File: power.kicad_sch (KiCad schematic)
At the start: 38 parts, among them IC3 LP5912-3.3DRVR, U12 BQ24075RGT, U2 LP5907SNX-1.8/NOPB, U3 LP5907SNX-3.3/NOPB, U4 LP5907SNX-1.8/NOPB, U6 LP5907SNX-3.3/NOPB, U7 LP5907SNX-3.3/NOPB

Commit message: segmented schematci
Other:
- note added: "BATTERY"
- note added: "BMS"
- note added: "REGULATORS"
- moved on the sheet: BT1, IC3

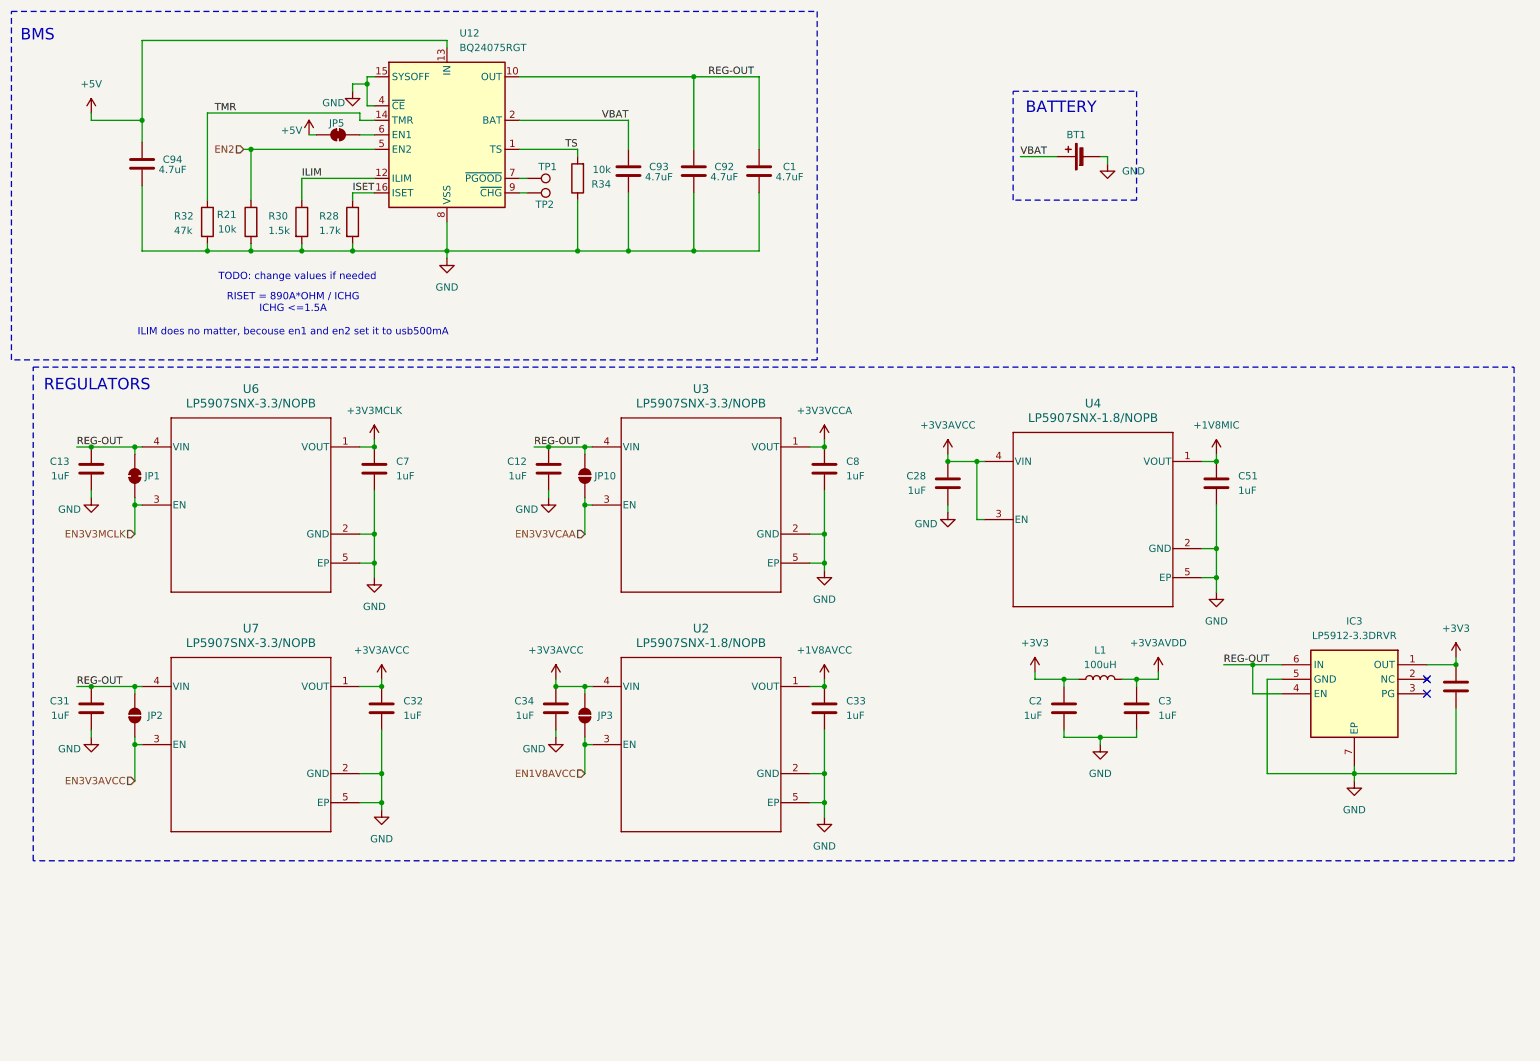
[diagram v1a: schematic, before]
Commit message: reannotated schematic
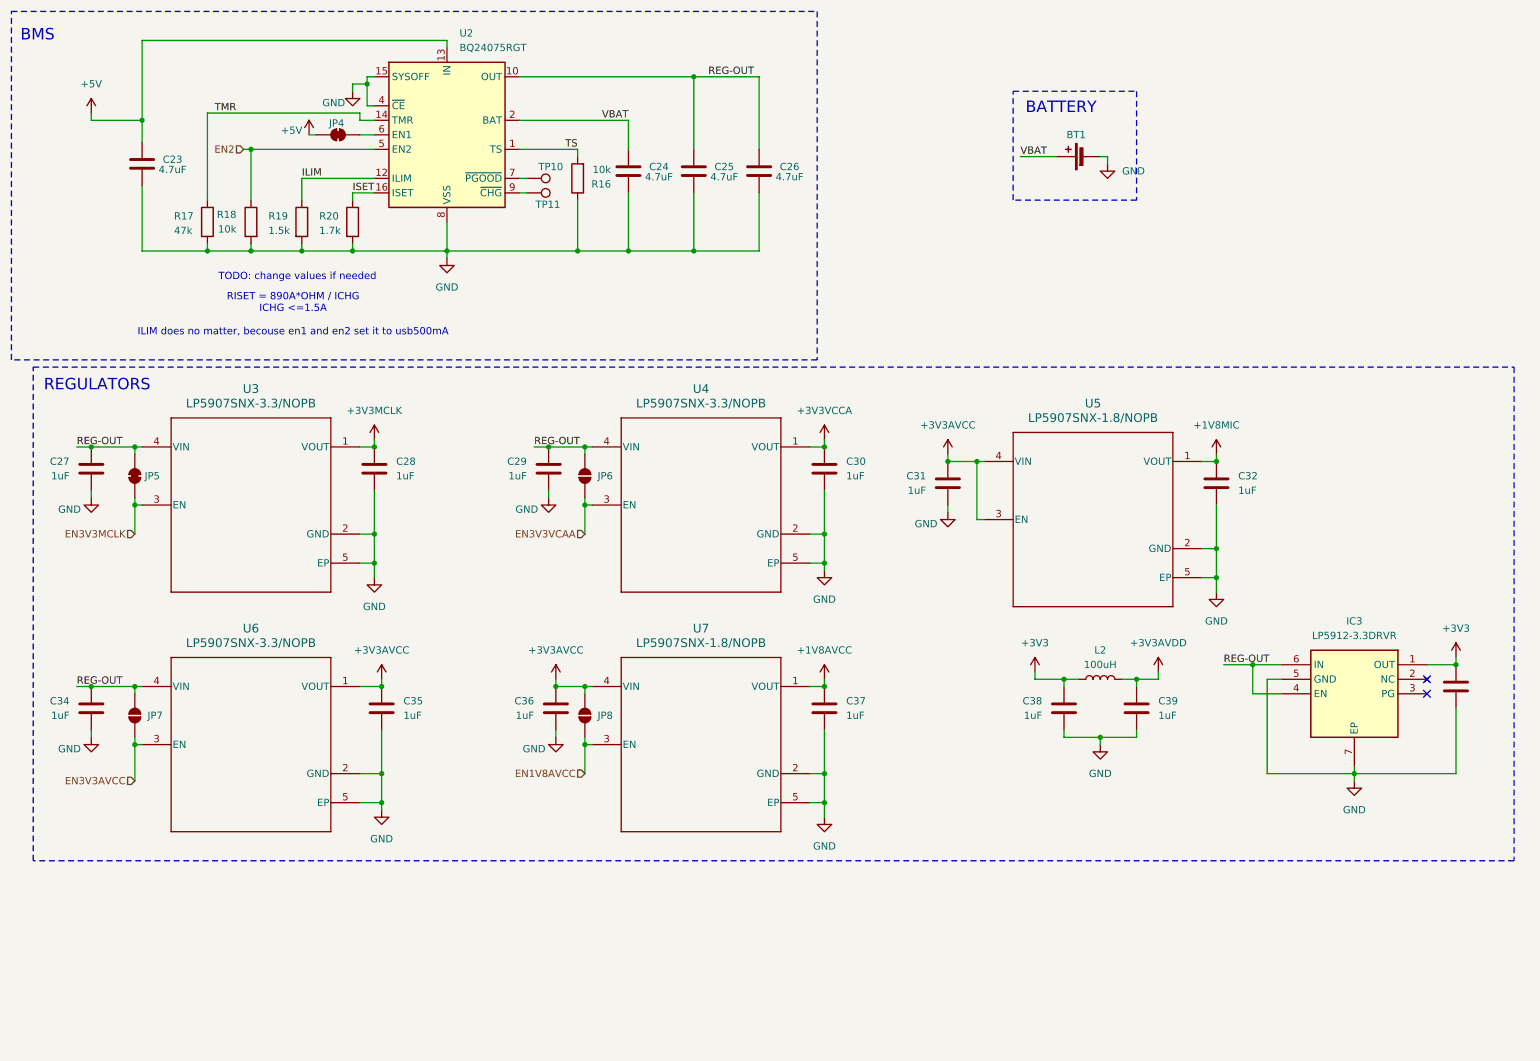
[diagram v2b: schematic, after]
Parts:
- renumbered C94 to C23, C93 to C24, C92 to C25, C1 to C26, C13 to C27, C7 to C28, C12 to C29, C8 to C30, C28 to C31, C51 to C32, C35 to C33, C31 to C34, C32 to C35, C34 to C36, C33 to C37, C2 to C38, C3 to C39, JP5 to JP4, JP1 to JP5, JP10 to JP6, JP2 to JP7, JP3 to JP8, L1 to L2, R34 to R16, R32 to R17, R21 to R18, R30 to R19, R28 to R20, TP1 to TP10, TP2 to TP11, U12 to U2, U6 to U3, U3 to U4, U4 to U5, U7 to U6, U2 to U7

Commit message: added titles to sheets
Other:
- title: (none) -> POWER
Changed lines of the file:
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@@
 	(generator_version "9.0")
 	(paper "A4")
+	(title_block
+		(title "POWER")
+	)
 	(rectangle
 		(start 19.05 76.2)

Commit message: small fixes
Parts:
- removed L2: 100uH, Inductor_SMD:L_TDK_MLZ2012_h1.25mm, symbol Device:L
- added JP10: SolderJumper_2_Open, Jumper:SolderJumper-2_P1.3mm_Open_RoundedPad1.0x1.5mm, symbol Jumper:SolderJumper_2_Open
- added U10: LP5907SNX-1.8/NOPB, Package_SON:Texas_X2SON-4_1x1mm_P0.65mm, symbol LP5907SNX-1-8-NOPB:LP5907SNX-1.8_NOPB
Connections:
- net +3V3: no longer C38.1
- net +3V3AVCC: now also C38.1, JP10.1 (A), U10.4 (VIN)
- net +3V3AVDD: now also U10.1 (VOUT)
- net GND: now also U10.2 (GND), U10.5 (EP)
- new net EN3V3AVDD: JP10.2 (B), U10.3 (EN)
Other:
- moved on the sheet: C31, C32, U5

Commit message: fuel gauge ic
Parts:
- added C57, C58, C59: 1uF, Capacitor_SMD:C_0402_1005Metric, symbol Device:C
- added IC5: BQ27427YZFR, BQ27427YZFR:BGA9C50P3X3_158X162X62, symbol BQ27427YZFR:BQ27427YZFR
- added R31: 10k, Resistor_SMD:R_0402_1005Metric, symbol Device:R
- C27, C28, C29, C30, C31, C32, C33, C34, C35, C36, C37, C38, C39: footprint (none) -> Capacitor_SMD:C_0402_1005Metric
- IC3: footprint SON65P200X200X80-7N -> LP5912-3.3DRVR:SON65P200X200X80-7N
- R18: footprint (none) -> Resistor_SMD:R_0402_1005Metric
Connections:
- net GND: now also C57.2, C58.2, C59.2, IC5.B2 (VSS_1), IC5.C1 (VSS_2), R31.1
- net REG-OUT: now also IC5.C2 (SRX)
- net VBAT renamed +BATT
- net +BATT: now also C59.1, IC5.C3 (BAT)
- new net: C57.1, C58.1, IC5.B3 (VDD)
- new net: IC5.B1 (BIN), R31.2
- new net FUEL_GPOUT: IC5.A1 (GPOUT)
- new net FUEL_SCL: IC5.A3 (SCL)
- new net FUEL_SDA: IC5.A2 (SDA)
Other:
- note added: "FUEAL GAUGE"
- note added: "POWER FLAGS"
- note added: "addr(dec.):85"
- moved on the sheet: BT1

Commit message: small stuff
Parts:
- added TP12, TP13, TP14, TP15, TP16, TP17, TP18: TestPoint, TestPoint:TestPoint_Pad_D1.5mm, symbol Connector:TestPoint
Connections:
- net +1V8AVCC: now also TP16.1
- net +1V8MIC: now also TP14.1
- net +3V3: now also TP17.1
- net +3V3AVCC: now also TP15.1
- net +3V3AVDD: now also TP18.1
- net +3V3MCLK: now also TP12.1
- net +3V3VCCA: now also TP13.1

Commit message: added models
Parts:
- BT1: footprint (none) -> S2B-PH-SM4-TB_LF__SN_:JST_S2B-PH-SM4-TB_LF__SN_
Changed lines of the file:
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@@
 			)
 		)
-		(property "Footprint" ""
+		(property "Footprint" "S2B-PH-SM4-TB_LF__SN_:JST_S2B-PH-SM4-TB_LF__SN_"
 			(at 268.986 59.69 90)
 			(effects

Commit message: started layout
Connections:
- net +3V3: now also C31.1, C38.1, JP10.1 (A), U10.4 (VIN), U5.3 (EN), U5.4 (VIN)
- net +3V3AVCC: no longer C31.1, C38.1, JP10.1 (A), U10.4 (VIN), U5.3 (EN), U5.4 (VIN)
